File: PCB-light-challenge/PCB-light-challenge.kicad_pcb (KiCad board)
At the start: 4 copper layers, 79.9 x 79 mm, 26 parts, among them J1 Conn_01x16_Socket, J3 Conn_01x13_Socket, U2 AP9101CK, U3 SP8K32FRATB

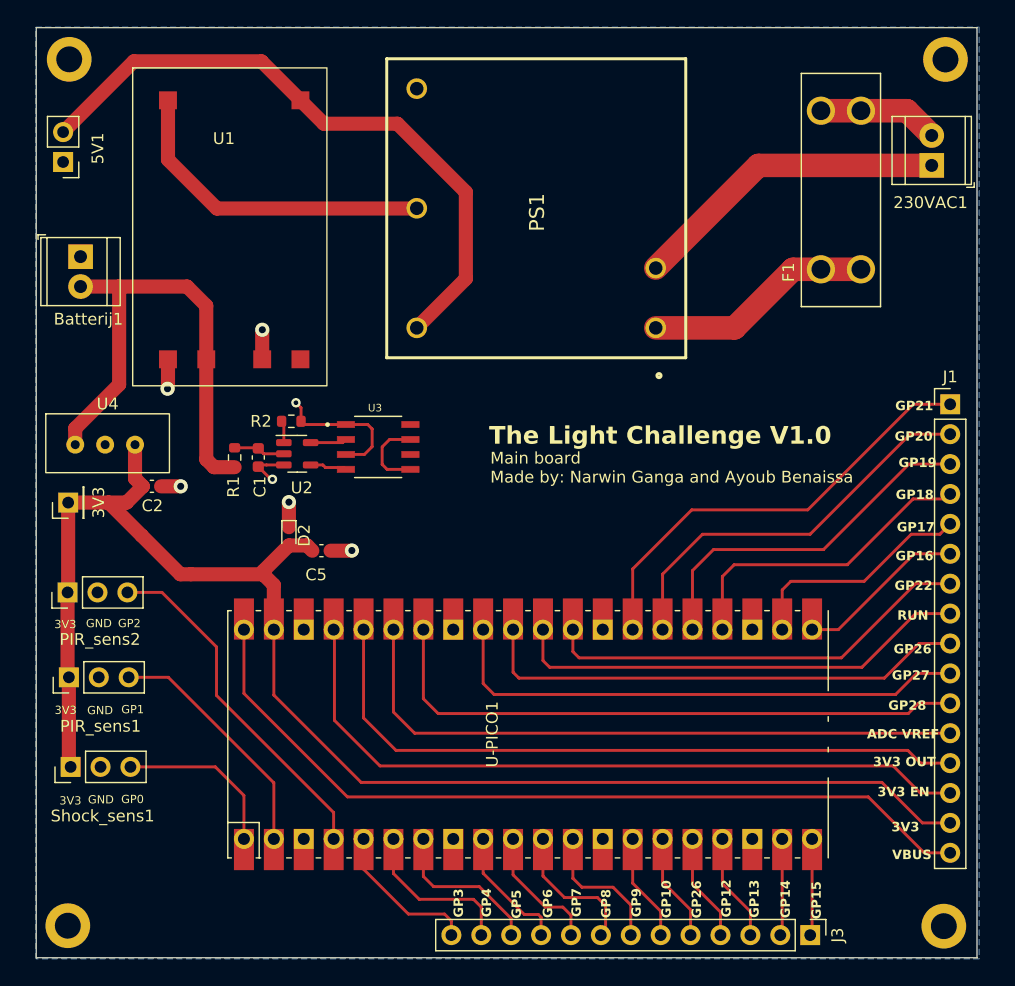
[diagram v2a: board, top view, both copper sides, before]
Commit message: PCB is AF en errors  fixed
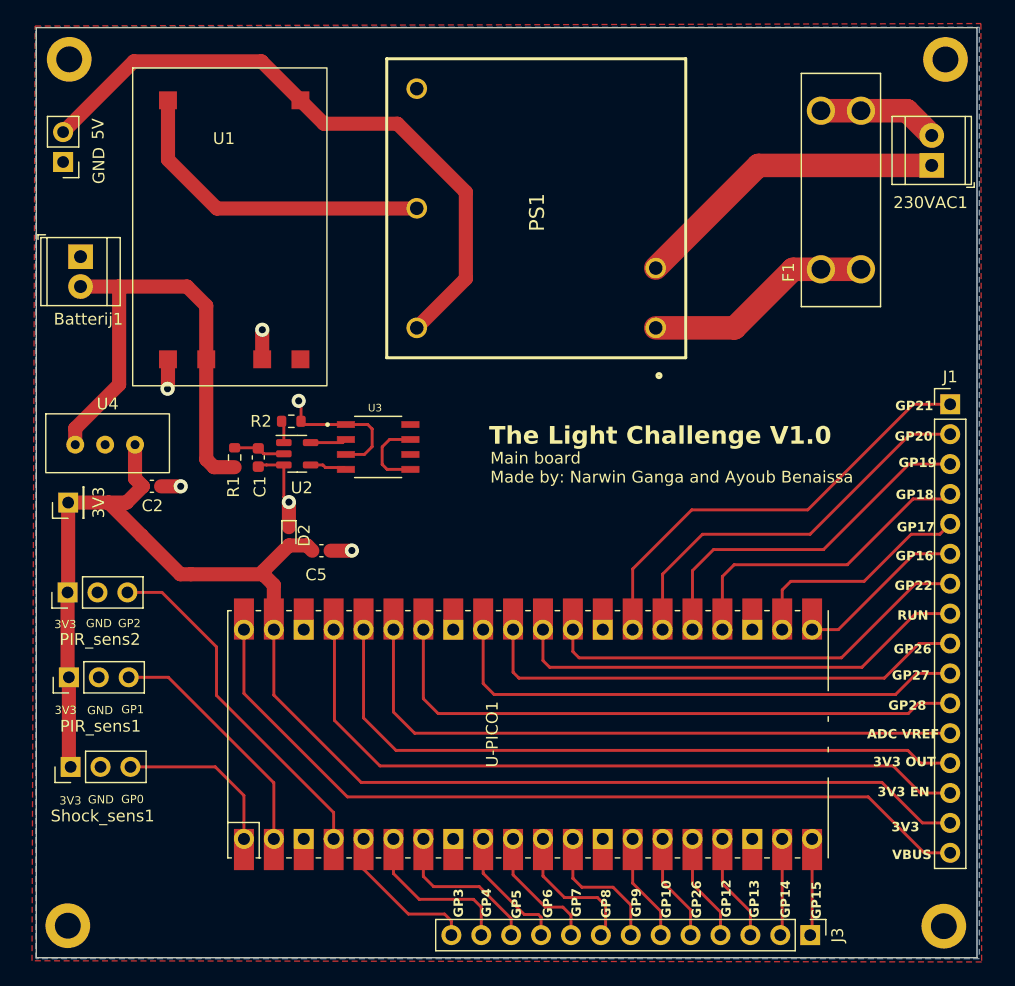
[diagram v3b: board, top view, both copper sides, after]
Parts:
- renumbered 5V1 to 5V
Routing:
- net GND: track 26.6 -> 28.3 mm, vias 7 -> 6
- added copper zone on F.Cu, net GND
- added copper zone on In2.Cu, net GND
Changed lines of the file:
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@@
     (property "ki_keywords" "connector")
     (attr through_hole)
-    (fp_text reference "5V1" (at -2.95 1.15 90) (layer "F.SilkS")
+    (fp_text reference "5V" (at -2.97 2.81 270) (layer "F.SilkS")
         (effects (font (size 1 1) (thickness 0.15)))
     )
@@
     (effects (font (size 0.8 0.8) (thickness 0.15) bold) (justify left bottom))
   )
+  (gr_text "GND" (at 177.76 84.85 90) (layer "F.SilkS")
+    (effects (font (size 1 1) (thickness 0.15)))
+  )
   (gr_text "GP27" (at 245.11 128.62) (layer "F.SilkS")
     (effects (font (size 0.8 0.8) (thickness 0.15) bold) (justify left bottom))
@@
   (gr_text "3V3 EN" (at 243.89 138.52) (layer "F.SilkS")
     (effects (font (size 0.8 0.8) (thickness 0.15) bold) (justify left bottom))
-  )
-  (dimension (type aligned) (layer "Edge.Cuts")
-    (pts (xy 172.4 73.1) (xy 172.77 152.22))
-    (height 6.67)
-    (gr_text "79,1209 mm" (at 167.06506 112.685814 270.2679384) (layer "Edge.Cuts")
-      (effects (font (size 1 1) (thickness 0.15)))
-    )
-    (format (prefix "") (suffix "") (units 3) (units_format 1) (precision 4))
-    (style (thickness 0.1) (arrow_length 1.27) (text_position_mode 0) (extension_height 0.58642) (extension_offset 0.5) keep_text_aligned)
-  )
-  (dimension (type aligned) (layer "Edge.Cuts")
-    (pts (xy 172.4 72.95) (xy 252.53 73.1))
-    (height -1.987)
-    (gr_text "80,1301 mm" (at 212.470873 69.888005 359.8927448) (layer "Edge.Cuts")
-      (effects (font (size 1 1) (thickness 0.15)))
-    )
-    (format (prefix "") (suffix "") (units 3) (units_format 1) (precision 4))
-    (style (thickness 0.1) (arrow_length 1.27) (text_position_mode 0) (extension_height 0.58642) (extension_offset 0.5) keep_text_aligned)
   )
   (segment (start 175.15 113.48) (end 178.59 113.48) (width 1.2) (layer "F.Cu") (net 1))
@@
   (segment (start 183.63 101.31) (end 183.63 103.77) (width 1.2) (layer "F.Cu") (net 41))
   (segment (start 191.44 110.285) (end 191.3 110.425) (width 0.25) (layer "F.Cu") (net 41))
-  (segment (start 194.93 105.43) (end 194.5 105) (width 0.25) (layer "F.Cu") (net 41))
-  (segment (start 192.5 111.5) (end 192.375 111.5) (width 0.25) (layer "F.Cu") (net 41))
   (segment (start 200.315 109.39) (end 200.97 108.735) (width 0.25) (layer "F.Cu") (net 41))
   (segment (start 197.44 117.57) (end 199.23 117.57) (width 1.2) (layer "F.Cu") (net 41))
   (segment (start 199.23 117.57) (end 199.25 117.55) (width 0.25) (layer "F.Cu") (net 41))
-  (segment (start 192.375 111.5) (end 191.3 110.425) (width 0.25) (layer "F.Cu") (net 41))
   (segment (start 191.63 101.31) (end 191.63 98.81) (width 1.2) (layer "F.Cu") (net 41))
   (segment (start 198.74 109.39) (end 200.315 109.39) (width 0.25) (layer "F.Cu") (net 41))
+  (segment (start 194.93 105.04) (end 194.73 104.84) (width 0.25) (layer "F.Cu") (net 41))
   (segment (start 195.205 106.85) (end 194.93 106.575) (width 0.25) (layer "F.Cu") (net 41))
-  (segment (start 194.93 106.575) (end 194.93 105.43) (width 0.25) (layer "F.Cu") (net 41))
   (segment (start 183.04 112.1) (end 184.71 112.1) (width 1.2) (layer "F.Cu") (net 41))
   (segment (start 192 110.285) (end 191.44 110.285) (width 0.25) (layer "F.Cu") (net 41))
+  (segment (start 193.47 113.01) (end 193.9 113.44) (width 0.25) (layer "F.Cu") (net 41))
   (segment (start 200.97 107.225) (end 200.595 106.85) (width 0.25) (layer "F.Cu") (net 41))
+  (segment (start 194.93 106.575) (end 194.93 105.04) (width 0.25) (layer "F.Cu") (net 41))
   (segment (start 193.47 110.285) (end 192 110.285) (width 0.25) (layer "F.Cu") (net 41))
+  (segment (start 193.47 110.285) (end 193.47 113.01) (width 0.25) (layer "F.Cu") (net 41))
   (segment (start 200.97 108.735) (end 200.97 107.225) (width 0.25) (layer "F.Cu") (net 41))
   (segment (start 193.9 113.44) (end 193.9 115.57) (width 1.2) (layer "F.Cu") (net 41))
   (segment (start 191.63 98.81) (end 191.64 98.8) (width 0.25) (layer "F.Cu") (net 41))
-  (via (at 192.5 111.5) (size 0.8) (drill 0.4) (layers "F.Cu" "B.Cu") (free) (net 41))
+  (via (at 194.73 104.84) (size 1.2) (drill 0.6) (layers "F.Cu" "B.Cu") (net 41))
   (via (at 199.25 117.55) (size 1.2) (drill 0.6) (layers "F.Cu" "B.Cu") (net 41))
   (via (at 193.9 113.44) (size 1.2) (drill 0.6) (layers "F.Cu" "B.Cu") (net 41))
-  (via (at 194.5 105) (size 0.8) (drill 0.4) (layers "F.Cu" "B.Cu") (net 41))
   (via (at 191.64 98.8) (size 1.2) (drill 0.6) (layers "F.Cu" "B.Cu") (net 41))
   (via (at 184.71 112.1) (size 1.2) (drill 0.6) (layers "F.Cu" "B.Cu") (net 41))
@@
   (segment (start 233.78 84.84) (end 225.06 93.56) (width 2) (layer "F.Cu") (net 46))
   (segment (start 248.5 84.84) (end 233.78 84.84) (width 2) (layer "F.Cu") (net 46))
+  (zone (net 41) (net_name "GND") (layer "F.Cu") (hatch edge 0.5)
+    (priority 2)
+    (connect_pads (clearance 0.5))
+    (min_thickness 0.25) (filled_areas_thickness no)
+    (fill yes (thermal_gap 0.5) (thermal_bridge_width 0.5))
+    (polygon
+      (pts
+        (xy 172.34 73)
+        (xy 252.68 72.79)
+        (xy 252.74 152.5)
+        (xy 172.08 152.4)
+        (xy 172.34 73.01)
+      )
+    )
+  )
   (zone (net 41) (net_name "GND") (layer "In1.Cu") (hatch edge 0.5)
     (connect_pads (clearance 0.5))
@@
       )
     )
+  )
+  (zone (net 41) (net_name "GND") (layer "In2.Cu") (hatch edge 0.5)
+    (priority 3)
+    (connect_pads (clearance 0.5))
+    (min_thickness 0.25) (filled_areas_thickness no)
+    (fill yes (thermal_gap 0.5) (thermal_bridge_width 0.5))
+    (polygon
+      (pts
+        (xy 172.34 73.01)
+        (xy 252.55 72.81)
+        (xy 252.65 152.47)
+        (xy 172.08 152.35)
+        (xy 172.34 73.02)
+      )
+    )
